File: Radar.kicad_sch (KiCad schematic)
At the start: 13 parts, among them J2 CON_5P, U2 XM125

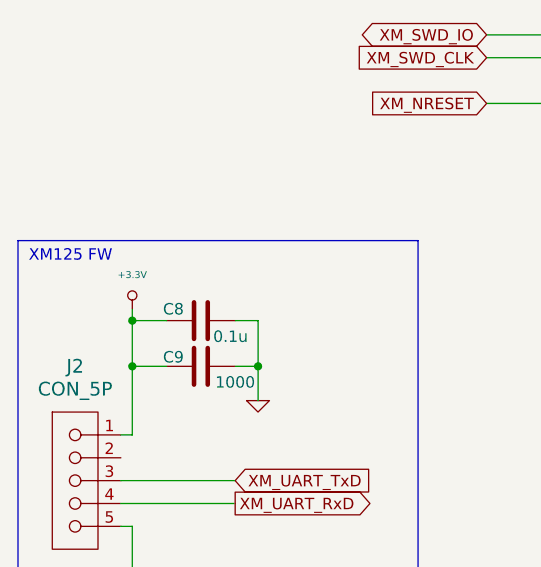
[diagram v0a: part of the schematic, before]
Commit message: DIP SW Pad Change
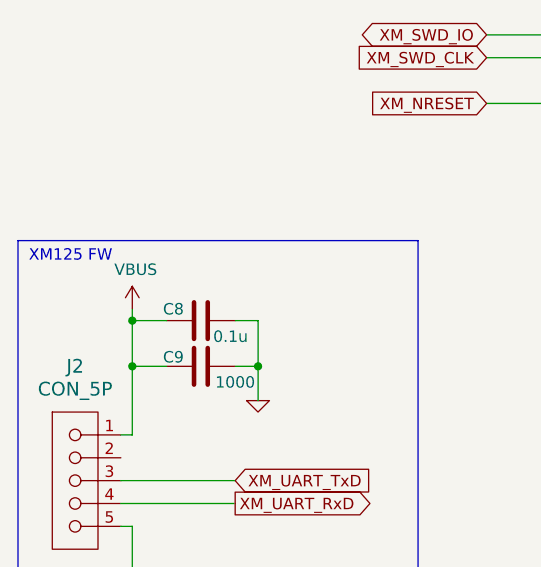
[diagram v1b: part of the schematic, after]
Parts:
- S4: footprint HLDC-E2:SW_DIP_SPSTx04_Slide_Omron_A6H-4101_W6.15mm_P1.27mm -> HLDC_E1:SOIC127P812X230-8N
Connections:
- net +3.3V: no longer C8.2, C9.2, J2.1
- new net VBUS: C8.2, C9.2, J2.1
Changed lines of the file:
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@@
+	)
+	(symbol
+		(lib_id "power:VCC")
+		(at 36.83 106.68 0)
+		(unit 1)
+		(exclude_from_sim no)
+		(in_bom yes)
+		(on_board yes)
+		(dnp no)
+		(property "Reference" "#PWR017"
+			(at 36.83 110.49 0)
+			(effects
+				(font
+					(size 1.27 1.27)
+				)
+				(hide yes)
+			)
+		)
+		(property "Value" "VBUS"
+			(at 37.211 102.2858 0)
+			(effects
+				(font
+					(size 1.27 1.27)
+				)
+			)
+		)
+		(property "Footprint" ""
+			(at 36.83 106.68 0)
+			(effects
+				(font
+					(size 1.27 1.27)
+				)
+				(hide yes)
+			)
+		)
+		(property "Datasheet" ""
+			(at 36.83 106.68 0)
+			(effects
+				(font
+					(size 1.27 1.27)
+				)
+				(hide yes)
+			)
+		)
+		(property "Description" ""
+			(at 36.83 106.68 0)
+			(effects
+				(font
+					(size 1.27 1.27)
+				)
+			)
+		)
+		(pin "1"
+		)
+		(instances
+			(project "Work"
+				(path "/6428906d-2278-429f-b11f-f65cfb2c8bcd/bca91c4a-b909-4000-9da3-d10e5b82a33b"
+					(reference "#PWR017")
+					(unit 1)
+				)
+			)
+		)
 	)
 	(symbol
@@
 			)
 		)
-		(property "Footprint" "HLDC-E2:SW_DIP_SPSTx04_Slide_Omron_A6H-4101_W6.15mm_P1.27mm"
+		(property "Footprint" "HLDC_E1:SOIC127P812X230-8N"
 			(at 232.41 147.32 0)
 			(effects
@@
 					(unit 1)
 				)
-			)
-		)
-	)
-	(symbol
-		(lib_id "HLDC_E1:+3.3V")
-		(at 36.83 106.68 0)
-		(unit 1)
-		(exclude_from_sim no)
-		(in_bom yes)
-		(on_board yes)
-		(dnp no)
-		(fields_autoplaced yes)
-		(property "Reference" "#PWR017"
-			(at 36.83 107.696 0)
-			(effects
-				(font
-					(size 0.762 0.762)
-				)
-				(hide yes)
-			)
-		)
-		(property "Value" "+3.3V"
-			(at 36.83 102.87 0)
-			(effects
-				(font
-					(size 0.762 0.762)
-				)
-			)
-		)
-		(property "Footprint" ""
-			(at 36.83 106.68 0)
-			(effects
-				(font
-					(size 1.524 1.524)
-				)
-			)
-		)
-		(property "Datasheet" ""
-			(at 36.83 106.68 0)
-			(effects
-				(font
-					(size 1.524 1.524)
-				)
-			)
-		)
-		(property "Description" ""
-			(at 36.83 106.68 0)
-			(effects
-				(font
-					(size 1.27 1.27)
-				)
-				(hide yes)
-			)
-		)
-		(pin "1"
-		)
-		(instances
-			(project "Work"
-				(path "/6428906d-2278-429f-b11f-f65cfb2c8bcd/bca91c4a-b909-4000-9da3-d10e5b82a33b"
-					(reference "#PWR017")
-					(unit 1)
-				)
